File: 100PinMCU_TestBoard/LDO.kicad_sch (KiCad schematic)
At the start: 5 parts, among them U2 MCP1826S

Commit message: pre japan flight
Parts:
- renumbered C9 to C10, C10 to C11, D12 to D14
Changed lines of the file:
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@@
 		(dnp no)
 		(fields_autoplaced yes)
-		(property "Reference" "C10"
+		(property "Reference" "C11"
 			(at 168.275 68.5735 0)
 			(effects
@@
 			(project "LDO"
 				(path "/abcdaa41-14f3-4587-9aac-314b09095246/ab199eb4-16ff-472f-a198-e557cdece1a6"
-					(reference "C10")
+					(reference "C11")
 					(unit 1)
 				)
@@
 		(dnp no)
 		(fields_autoplaced yes)
-		(property "Reference" "D12"
+		(property "Reference" "D14"
 			(at 133.604 57.15 0)
 			(effects
@@
 			(project ""
 				(path "/abcdaa41-14f3-4587-9aac-314b09095246/ab199eb4-16ff-472f-a198-e557cdece1a6"
-					(reference "D12")
+					(reference "D14")
 					(unit 1)
 				)
@@
 		(dnp no)
 		(fields_autoplaced yes)
-		(property "Reference" "C9"
+		(property "Reference" "C10"
 			(at 142.875 68.5735 0)
 			(effects
@@
 			(project "LDO"
 				(path "/abcdaa41-14f3-4587-9aac-314b09095246/ab199eb4-16ff-472f-a198-e557cdece1a6"
-					(reference "C9")
-					(unit 1)
-				)
+					(reference "C10")
+					(unit 1)
+				)

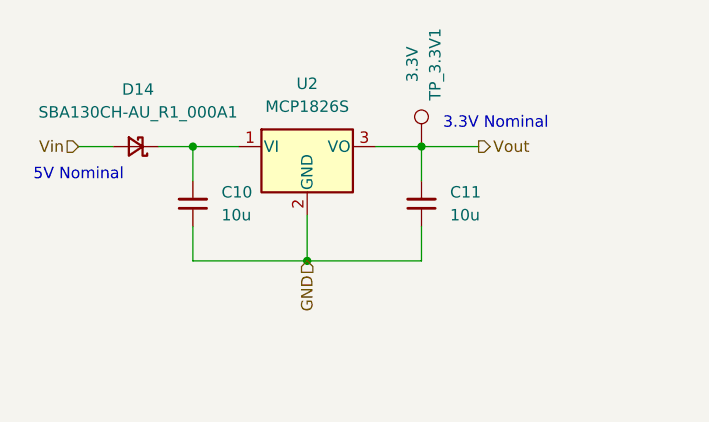
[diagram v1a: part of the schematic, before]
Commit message: add mux
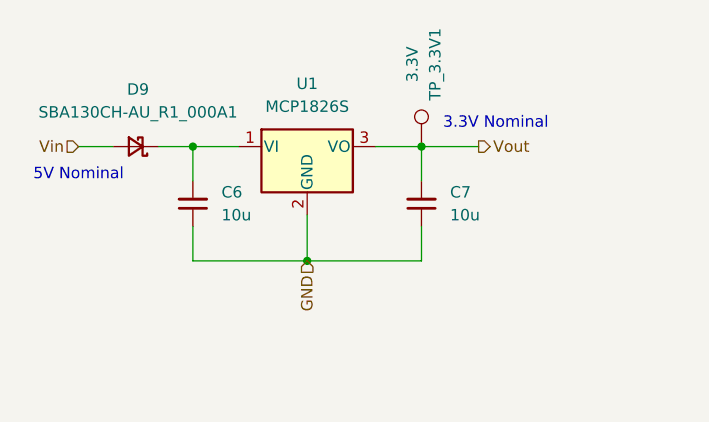
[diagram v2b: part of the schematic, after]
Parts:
- renumbered C10 to C6, C11 to C7, D14 to D9, U2 to U1
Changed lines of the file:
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@@
 		(dnp no)
 		(fields_autoplaced yes)
-		(property "Reference" "C11"
+		(property "Reference" "C7"
 			(at 168.275 68.5735 0)
 			(effects
@@
 		)
 		(instances
-			(project "LDO"
-				(path "/8ff43370-8d10-4d2c-b1a3-81d1c2934a98"
-					(reference "C2")
-					(unit 1)
-				)
-			)
-			(project "LDO"
-				(path "/abcdaa41-14f3-4587-9aac-314b09095246/ab199eb4-16ff-472f-a198-e557cdece1a6"
-					(reference "C11")
-					(unit 1)
-				)
-			)
-			(project "LeaderSOMBreakout"
-				(path "/e5b32072-3e3d-42a6-9d41-1a76d538e329/f3053c74-1ac6-4a33-80f3-565e8c4c2c7d"
-					(reference "C?")
+			(project "100PinMCU_ESP32_TestBoard"
+				(path "/abcdaa41-14f3-4587-9aac-314b09095246/e2002d7a-6f47-446e-bd1b-89d63ee3a45c"
+					(reference "C7")
 					(unit 1)
 				)
@@
 		)
 		(instances
-			(project "LDO"
-				(path "/8ff43370-8d10-4d2c-b1a3-81d1c2934a98"
-					(reference "TP_3.3V1")
-					(unit 1)
-				)
-			)
-			(project "LDO"
-				(path "/abcdaa41-14f3-4587-9aac-314b09095246/ab199eb4-16ff-472f-a198-e557cdece1a6"
+			(project "100PinMCU_ESP32_TestBoard"
+				(path "/abcdaa41-14f3-4587-9aac-314b09095246/e2002d7a-6f47-446e-bd1b-89d63ee3a45c"
 					(reference "TP_3.3V1")
 					(unit 1)
@@
 		(dnp no)
 		(fields_autoplaced yes)
-		(property "Reference" "U2"
+		(property "Reference" "U1"
 			(at 152.4 56.515 0)
 			(effects
@@
 		)
 		(instances
-			(project ""
-				(path "/8ff43370-8d10-4d2c-b1a3-81d1c2934a98"
+			(project "100PinMCU_ESP32_TestBoard"
+				(path "/abcdaa41-14f3-4587-9aac-314b09095246/e2002d7a-6f47-446e-bd1b-89d63ee3a45c"
 					(reference "U1")
-					(unit 1)
-				)
-			)
-			(project ""
-				(path "/abcdaa41-14f3-4587-9aac-314b09095246/ab199eb4-16ff-472f-a198-e557cdece1a6"
-					(reference "U2")
 					(unit 1)
 				)
@@
 		(dnp no)
 		(fields_autoplaced yes)
-		(property "Reference" "D14"
+		(property "Reference" "D9"
 			(at 133.604 57.15 0)
 			(effects
@@
 		)
 		(instances
-			(project ""
-				(path "/8ff43370-8d10-4d2c-b1a3-81d1c2934a98"
-					(reference "D1")
-					(unit 1)
-				)
-			)
-			(project ""
-				(path "/abcdaa41-14f3-4587-9aac-314b09095246/ab199eb4-16ff-472f-a198-e557cdece1a6"
-					(reference "D14")
+			(project "100PinMCU_ESP32_TestBoard"
+				(path "/abcdaa41-14f3-4587-9aac-314b09095246/e2002d7a-6f47-446e-bd1b-89d63ee3a45c"
+					(reference "D9")
 					(unit 1)
 				)
@@
 		(dnp no)
 		(fields_autoplaced yes)
-		(property "Reference" "C10"
+		(property "Reference" "C6"
 			(at 142.875 68.5735 0)
 			(effects
@@
 		)
 		(instances
-			(project "LDO"
-				(path "/8ff43370-8d10-4d2c-b1a3-81d1c2934a98"
-					(reference "C1")
+			(project "100PinMCU_ESP32_TestBoard"
+				(path "/abcdaa41-14f3-4587-9aac-314b09095246/e2002d7a-6f47-446e-bd1b-89d63ee3a45c"
+					(reference "C6")
 					(unit 1)
 				)
-			)
-			(project "LDO"
-				(path "/abcdaa41-14f3-4587-9aac-314b09095246/ab199eb4-16ff-472f-a198-e557cdece1a6"
-					(reference "C10")
-					(unit 1)
-				)
-			)
-			(project ""
-				(path "/e5b32072-3e3d-42a6-9d41-1a76d538e329/f3053c74-1ac6-4a33-80f3-565e8c4c2c7d"
-					(reference "C?")
-					(unit 1)
-				)

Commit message: erc
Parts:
- renumbered C7 to C10, C6 to C9, D9 to D12, U1 to U2
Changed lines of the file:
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@@
 		(dnp no)
 		(fields_autoplaced yes)
-		(property "Reference" "C7"
+		(property "Reference" "C10"
 			(at 168.275 68.5735 0)
 			(effects
@@
 			(project "100PinMCU_ESP32_TestBoard"
 				(path "/abcdaa41-14f3-4587-9aac-314b09095246/e2002d7a-6f47-446e-bd1b-89d63ee3a45c"
-					(reference "C7")
+					(reference "C10")
 					(unit 1)
 				)
@@
 		(dnp no)
 		(fields_autoplaced yes)
-		(property "Reference" "U1"
+		(property "Reference" "U2"
 			(at 152.4 56.515 0)
 			(effects
@@
 			(project "100PinMCU_ESP32_TestBoard"
 				(path "/abcdaa41-14f3-4587-9aac-314b09095246/e2002d7a-6f47-446e-bd1b-89d63ee3a45c"
-					(reference "U1")
+					(reference "U2")
 					(unit 1)
 				)
@@
 		(dnp no)
 		(fields_autoplaced yes)
-		(property "Reference" "D9"
+		(property "Reference" "D12"
 			(at 133.604 57.15 0)
 			(effects
@@
 			(project "100PinMCU_ESP32_TestBoard"
 				(path "/abcdaa41-14f3-4587-9aac-314b09095246/e2002d7a-6f47-446e-bd1b-89d63ee3a45c"
-					(reference "D9")
+					(reference "D12")
 					(unit 1)
 				)
@@
 		(dnp no)
 		(fields_autoplaced yes)
-		(property "Reference" "C6"
+		(property "Reference" "C9"
 			(at 142.875 68.5735 0)
 			(effects
@@
 			(project "100PinMCU_ESP32_TestBoard"
 				(path "/abcdaa41-14f3-4587-9aac-314b09095246/e2002d7a-6f47-446e-bd1b-89d63ee3a45c"
-					(reference "C6")
+					(reference "C9")
 					(unit 1)
 				)
